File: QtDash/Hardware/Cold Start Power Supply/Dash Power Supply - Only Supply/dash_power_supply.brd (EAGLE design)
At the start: 50.8 x 45.4 mm, 24 parts, among them IC2 LM3488, Q4 BSC027N04LSG

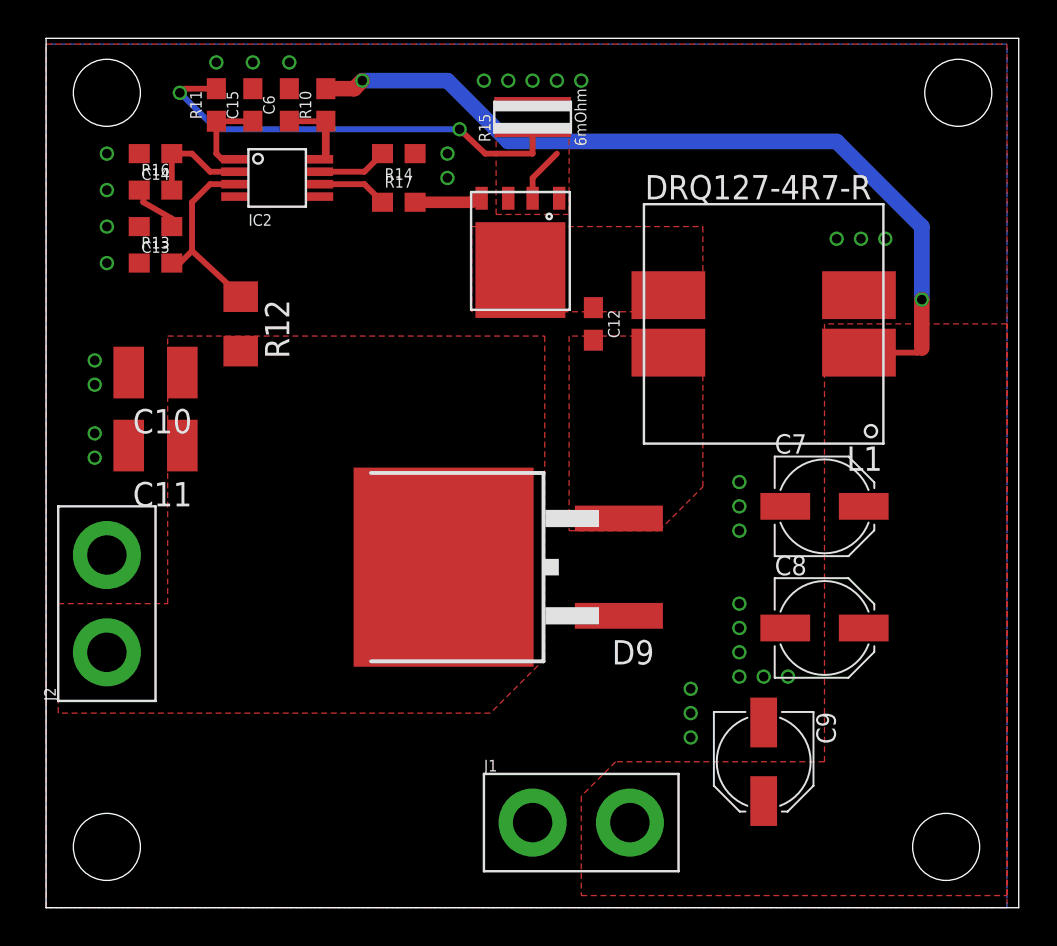
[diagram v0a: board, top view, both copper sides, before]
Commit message: topic/component-optimization: 	- 20k resistor on vin of power supply should have been 20R 	- fixed silk screen on cold start power supply 	- re-arranged components a via for cleaner return paths
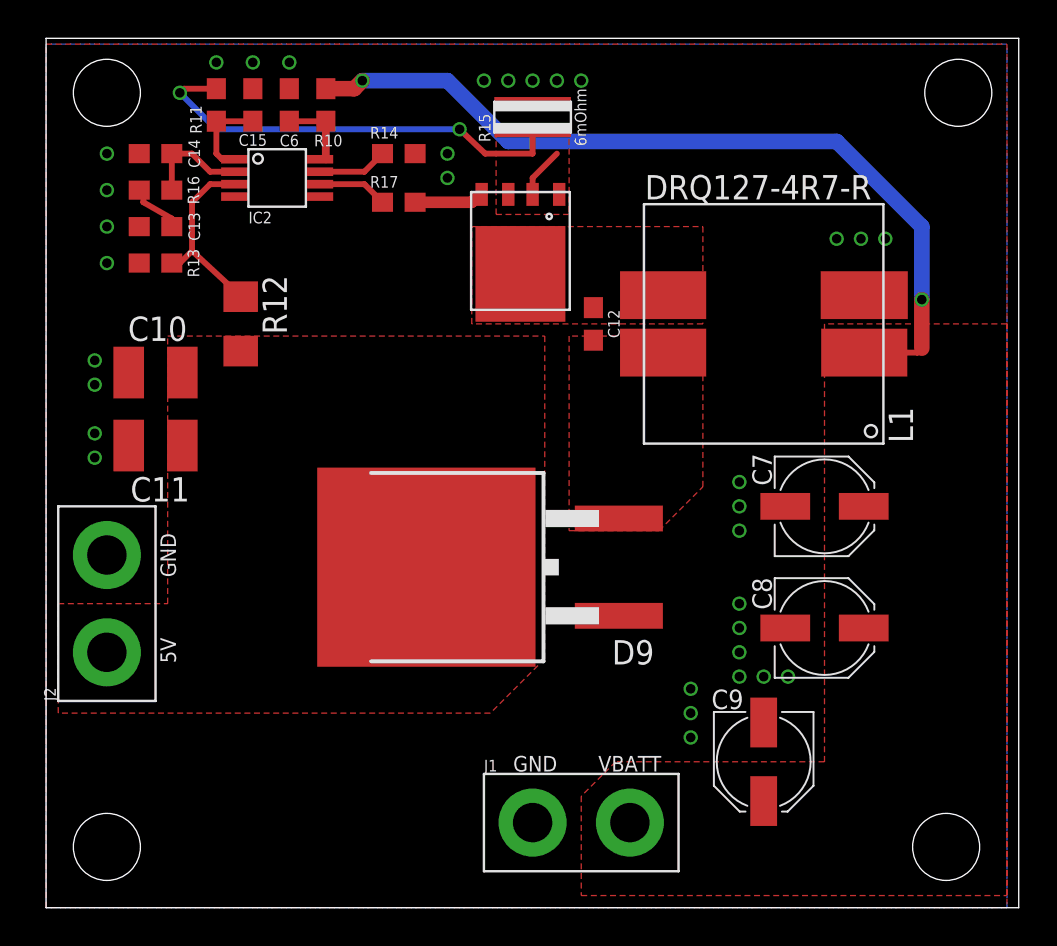
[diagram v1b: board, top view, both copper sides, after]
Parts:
- R10: value 20k -> 20R
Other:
- board text added: "5V"
- board text added: "GND"
- board text added: "VBATT"

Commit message: topic/component-optimization: 	- small changes to cold start power supply
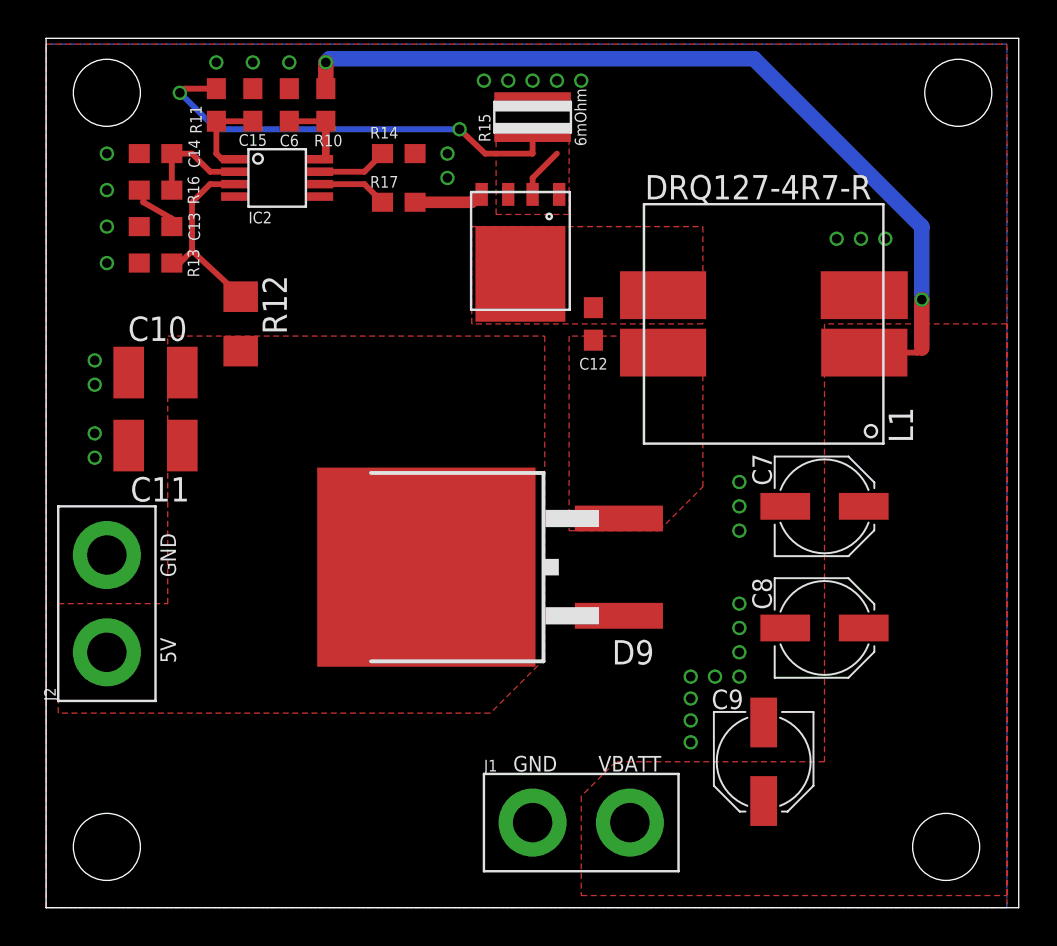
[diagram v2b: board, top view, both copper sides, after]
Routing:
- net VBATT: track 43.9 -> 45.6 mm
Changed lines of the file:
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@@
 <element name="C12" library="digital_dash" package="0603" value="4.7u" x="28.575" y="30.48" smashed="yes" rot="R270">
 <attribute name="VOLTAGE" value="35V" x="28.575" y="30.48" size="1.778" layer="27" rot="R270" display="off"/>
-<attribute name="NAME" x="29.337" y="30.48" size="0.6096" layer="25" font="vector" ratio="20" rot="R270" align="bottom-center"/>
+<attribute name="NAME" x="28.575" y="28.702" size="0.6096" layer="25" font="vector" ratio="20" rot="R180" align="bottom-center"/>
 <attribute name="VALUE" x="27.813" y="30.48" size="0.6096" layer="27" font="vector" ratio="20" rot="R270" align="top-center"/>
 </element>
@@
 <wire x1="42.715" y1="28.98" x2="45.49" y2="28.98" width="0.3048" layer="1"/>
 <wire x1="45.49" y1="28.98" x2="45.72" y2="29.21" width="0.3048" layer="1"/>
-<via x="16.51" y="43.18" extent="1-16" drill="0.5"/>
+<via x="14.605" y="44.1325" extent="1-16" drill="0.5"/>
 <via x="45.72" y="31.75" extent="1-16" drill="0.5"/>
 <wire x1="45.72" y1="31.75" x2="45.72" y2="29.21" width="0.8128" layer="1"/>
@@
 <vertex x="27.94" y="5.82395"/>
 </polygon>
-<wire x1="16.51" y1="43.18" x2="16.09" y2="42.76" width="0.8128" layer="1"/>
-<wire x1="16.09" y1="42.76" x2="14.605" y2="42.76" width="0.8128" layer="1"/>
 <wire x1="45.72" y1="31.75" x2="45.72" y2="35.56" width="0.8128" layer="16"/>
-<wire x1="45.72" y1="35.56" x2="41.275" y2="40.005" width="0.8128" layer="16"/>
-<wire x1="41.275" y1="40.005" x2="24.13" y2="40.005" width="0.8128" layer="16"/>
-<wire x1="24.13" y1="40.005" x2="20.955" y2="43.18" width="0.8128" layer="16"/>
-<wire x1="20.955" y1="43.18" x2="16.51" y2="43.18" width="0.8128" layer="16"/>
+<wire x1="45.72" y1="35.56" x2="36.957" y2="44.323" width="0.8128" layer="16"/>
 <contactref element="J1" pad="2"/>
+<wire x1="36.957" y1="44.323" x2="14.7955" y2="44.323" width="0.8128" layer="16"/>
+<wire x1="14.7955" y1="44.323" x2="14.605" y2="44.1325" width="0.8128" layer="16"/>
+<wire x1="14.605" y1="44.1325" x2="14.605" y2="42.76" width="0.8128" layer="1"/>
 </signal>
 <signal name="GND">
@@
 </polygon>
 <contactref element="J2" pad="2"/>
-<via x="33.655" y="8.89" extent="1-16" drill="0.5"/>
-<via x="33.655" y="10.16" extent="1-16" drill="0.5"/>
-<via x="33.655" y="11.43" extent="1-16" drill="0.5"/>
+<via x="33.655" y="9.779" extent="1-16" drill="0.5"/>
+<via x="33.655" y="10.922" extent="1-16" drill="0.5"/>
+<via x="33.655" y="12.065" extent="1-16" drill="0.5"/>
 <via x="36.195" y="14.605" extent="1-16" drill="0.5"/>
 <via x="36.195" y="15.875" extent="1-16" drill="0.5"/>
 <via x="36.195" y="13.335" extent="1-16" drill="0.5"/>
 <via x="36.195" y="12.065" extent="1-16" drill="0.5"/>
-<via x="37.465" y="12.065" extent="1-16" drill="0.5"/>
-<via x="38.735" y="12.065" extent="1-16" drill="0.5"/>
 <via x="36.195" y="22.225" extent="1-16" drill="0.5"/>
 <via x="36.195" y="20.955" extent="1-16" drill="0.5"/>
@@
 <via x="12.7" y="44.1325" extent="1-16" drill="0.5"/>
 <contactref element="J1" pad="1"/>
+<via x="34.925" y="12.065" extent="1-16" drill="0.5"/>
+<via x="33.655" y="8.636" extent="1-16" drill="0.5"/>
 </signal>
 <signal name="N$12">
@@
 <wire x1="21.59" y1="40.64" x2="22.925" y2="39.37" width="0.3048" layer="1"/>
 <wire x1="22.925" y1="39.37" x2="25.4" y2="39.37" width="0.3048" layer="1"/>
-<wire x1="25.4" y1="39.37" x2="25.4" y2="40.575" width="0.3048" layer="1"/>
+<wire x1="25.4" y1="39.37" x2="25.4" y2="40.475" width="0.3048" layer="1"/>
 <wire x1="6.985" y1="42.545" x2="7.2" y2="42.76" width="0.3048" layer="1"/>
 <wire x1="7.2" y1="42.76" x2="8.89" y2="42.76" width="0.3048" layer="1"/>

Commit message: topic/component-optimization: 	- added some more output capacitors
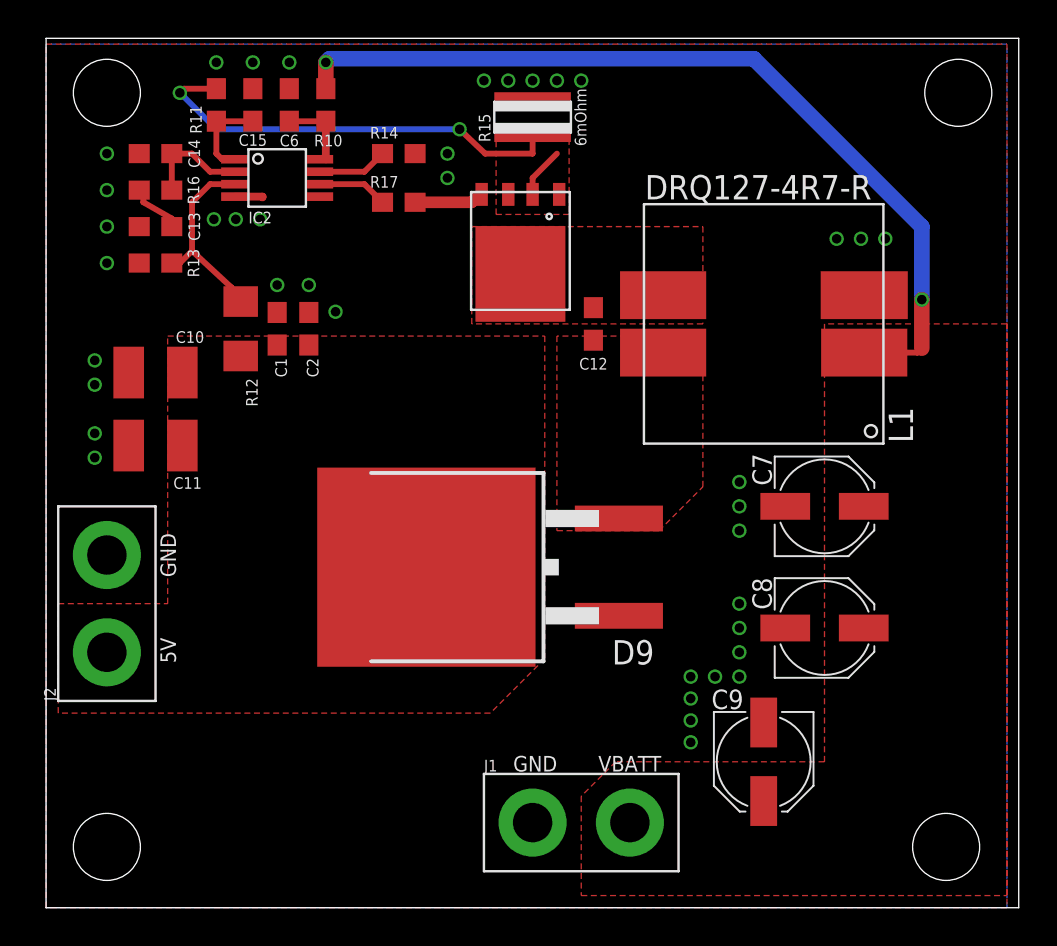
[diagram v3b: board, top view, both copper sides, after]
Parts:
- added C1: 100n, digital_dash:0603
- added C2: 4.7u, digital_dash:0603
- moved R12 0.25 mm to (10.2, 30.2)
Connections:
- net 5V: now also C1.1, C2.1
- net GND: now also C1.2, C2.2
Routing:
- net GND: track 0.00 -> 1.48 mm, vias 33 -> 39
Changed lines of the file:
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@@
 <attribute name="VALUE" x="9.652" y="41.91" size="0.6096" layer="27" font="vector" ratio="20" rot="R90" align="top-center"/>
 </element>
-<element name="R12" library="dash_power_supply" package="R1206" value="30.9k 1%" x="10.16" y="30.48" smashed="yes" rot="R270">
-<attribute name="POWER" value=".25W" x="10.16" y="30.48" size="1.778" layer="27" rot="R270" display="off"/>
-<attribute name="NAME" x="11.303" y="33.02" size="1.27" layer="25" rot="R270"/>
-<attribute name="VALUE" x="7.62" y="31.75" size="1.27" layer="27" rot="R270"/>
+<element name="R12" library="dash_power_supply" package="R1206" value="30.9k 1%" x="10.16" y="30.226" smashed="yes" rot="R270">
+<attribute name="POWER" value=".25W" x="10.16" y="30.226" size="1.778" layer="27" rot="R270" display="off"/>
+<attribute name="NAME" x="11.049" y="26.162" size="0.6096" layer="25" font="vector" ratio="20" rot="R90"/>
+<attribute name="VALUE" x="7.62" y="31.496" size="1.27" layer="27" rot="R270"/>
 </element>
 <element name="R14" library="SparkFun-Resistors" package="0603" value="75k" x="18.415" y="39.37" smashed="yes" rot="R180">
@@
 <element name="C10" library="dash_power_supply" package="C1210" value="100u" x="5.715" y="27.94" smashed="yes" rot="R180">
 <attribute name="VOLTAGE" value="10V" x="5.715" y="27.94" size="1.778" layer="27" rot="R180" display="off"/>
-<attribute name="NAME" x="7.366" y="30.861" size="1.27" layer="25" rot="R180"/>
+<attribute name="NAME" x="8.255" y="30.099" size="0.6096" layer="25" font="vector" ratio="20" rot="R180"/>
 <attribute name="VALUE" x="7.62" y="31.115" size="1.27" layer="27" rot="R180"/>
 </element>
 <element name="C11" library="dash_power_supply" package="C1210" value="100u" x="5.715" y="24.13" smashed="yes" rot="R180">
 <attribute name="VOLTAGE" value="10V" x="5.715" y="24.13" size="1.778" layer="27" rot="R180" display="off"/>
-<attribute name="NAME" x="7.493" y="22.479" size="1.27" layer="25" rot="R180"/>
+<attribute name="NAME" x="8.128" y="22.479" size="0.6096" layer="25" font="vector" ratio="20" rot="R180"/>
 <attribute name="VALUE" x="7.62" y="27.305" size="1.27" layer="27" rot="R180"/>
 </element>
@@
 <element name="J2" library="SparkFun-Connectors" package="1X02_XTRA_BIG" value="" x="3.175" y="15.875" rot="R90"/>
 <element name="J1" library="SparkFun-Connectors" package="1X02_XTRA_BIG" value="" x="27.94" y="4.445"/>
+<element name="C1" library="digital_dash" package="0603" value="100n" x="12.065" y="30.226" smashed="yes" rot="R90">
+<attribute name="VOLTAGE" value="50V" x="12.065" y="30.226" size="1.778" layer="27" rot="R90" display="off"/>
+<attribute name="NAME" x="12.573" y="28.194" size="0.6096" layer="25" font="vector" ratio="20" rot="R90" align="bottom-center"/>
+<attribute name="VALUE" x="12.827" y="30.226" size="0.6096" layer="27" font="vector" ratio="20" rot="R90" align="top-center"/>
+</element>
+<element name="C2" library="digital_dash" package="0603" value="4.7u" x="13.716" y="30.226" smashed="yes" rot="R90">
+<attribute name="VOLTAGE" value="35V" x="13.716" y="30.226" size="1.778" layer="27" rot="R90" display="off"/>
+<attribute name="NAME" x="14.224" y="28.194" size="0.6096" layer="25" font="vector" ratio="20" rot="R90" align="bottom-center"/>
+<attribute name="VALUE" x="14.478" y="30.226" size="0.6096" layer="27" font="vector" ratio="20" rot="R90" align="top-center"/>
+</element>
 </elements>
 <signals>
@@
 <via x="34.925" y="12.065" extent="1-16" drill="0.5"/>
 <via x="33.655" y="8.636" extent="1-16" drill="0.5"/>
+<contactref element="C2" pad="2"/>
+<contactref element="C1" pad="2"/>
+<wire x1="9.865" y1="37.125" x2="11.303" y2="37.125" width="0.4064" layer="1"/>
+<wire x1="11.303" y1="37.125" x2="11.303" y2="37.084" width="0.4064" layer="1"/>
+<via x="9.906" y="35.941" extent="1-16" drill="0.5"/>
+<via x="8.763" y="35.941" extent="1-16" drill="0.5"/>
+<via x="11.176" y="35.941" extent="1-16" drill="0.5"/>
+<via x="12.065" y="32.512" extent="1-16" drill="0.5"/>
+<via x="13.716" y="32.512" extent="1-16" drill="0.5"/>
+<via x="15.113" y="31.115" extent="1-16" drill="0.5"/>
 </signal>
 <signal name="N$12">
@@
 <wire x1="6.985" y1="33.655" x2="6.565" y2="33.655" width="0.3048" layer="1"/>
 <wire x1="7.62" y1="34.29" x2="9.677" y2="32.385" width="0.3048" layer="1"/>
-<wire x1="9.677" y1="32.385" x2="10.16" y2="31.902" width="0.3048" layer="1"/>
+<wire x1="9.677" y1="32.385" x2="10.16" y2="31.648" width="0.3048" layer="1"/>
 </signal>
 <signal name="N$19">
@@
 <polygon width="0.3048" layer="1" isolate="0.3048" thermals="no" rank="2">
 <vertex x="34.29" y="29.845"/>
-<vertex x="27.305" y="29.845"/>
-<vertex x="27.305" y="19.685"/>
+<vertex x="26.67" y="29.845"/>
+<vertex x="26.67" y="19.685"/>
 <vertex x="32.000475" y="19.685"/>
 <vertex x="34.29" y="21.974525"/>
@@
 </polygon>
 <contactref element="J2" pad="1"/>
+<contactref element="C1" pad="1"/>
+<contactref element="C2" pad="1"/>
 </signal>
 <signal name="N$11">

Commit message: topic/component-optimization: 	- rev b of cold start supply ordered
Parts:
- moved C7 6.91 mm to (34.2, 18.5)
- moved C8 6.75 mm to (34.2, 12.7)
- moved C9 4.83 mm to (33.1, 5.46)
- moved L1 4.83 mm to (33.1, 28.3)
- moved Q4 4.83 mm to (20.4, 32.1)
- moved D9 4.83 mm to (19.8, 15.6)
- moved C12 4.83 mm to (24.3, 28.3)
- moved R15 4.83 mm to (21.1, 39.1)
- moved J1 4.70 mm to (23.5, 2.92)
- moved R17 3.15 mm to (16.4, 34.4), turned to 270 degrees
- moved R16 2.16 mm to (5.71, 35.3)
- moved C10 2.16 mm to (5.71, 25.8)
- moved R13 2.16 mm to (5.71, 31.5)
- moved J2 2.16 mm to (3.17, 13.7)
- moved C1 2.16 mm to (12.1, 28.1)
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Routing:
- net N$17: track 25.5 -> 20.7 mm
- net VBATT: track 45.6 -> 41.3 mm
- net N$15: track 3.69 -> 2.26 mm
- net N$11: track 3.62 -> 3.11 mm
- net GND: vias 39 -> 43
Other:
- board size 50.8 x 45.4 mm -> 43.8 x 43.2 mm
- board text added: "Cold Start Power Supply VIN: 3-24V VOUT: 5.1V Rev B Mar 2022 @whitfijs"

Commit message: 82-bom-missing: 	- added BOM for eagle version of the power supply
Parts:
- Q4: value BSC027N04LSG -> DMTH6002LPS-13
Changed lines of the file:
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@@
 <attribute name="VALUE" x="15.621" y="34.417" size="0.6096" layer="27" font="vector" ratio="20" rot="R270" align="top-center"/>
 </element>
-<element name="Q4" library="dash_power_supply" package="TDSON" value="BSC027N04LSG" x="20.447" y="32.131" smashed="yes" rot="R270"/>
+<element name="Q4" library="dash_power_supply" package="TDSON" value="DMTH6002LPS-13" x="20.447" y="32.131" smashed="yes" rot="R270"/>
 <element name="C13" library="digital_dash" package="0603" value=".68u" x="5.715" y="33.401" smashed="yes" rot="R180">
 <attribute name="VOLTAGE" value="16V" x="5.715" y="33.401" size="1.778" layer="27" rot="R180" display="off"/>
